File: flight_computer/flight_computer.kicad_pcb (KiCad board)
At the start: 4 copper layers, 47 x 66 mm, 102 parts, among them J1 Conn_02x05_Odd_Even, J2 MEM2061-01-188-00-A_REVA, J3 Conn_01x02, J5 3817564, J7 Conn_01x07_MountingPin, Q1 Q_NPN_BEC, Q2 Q_NMOS_GSD, SW1 SW_Push, SW2 SW_Push, U1 STM8S007C8T6TR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

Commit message: a routing attempt
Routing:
- net /SPI_SCK: track 0.00 -> 50.1 mm, vias 0 -> 3
- net /SCL: track 2.18 -> 50.0 mm, vias 0 -> 2
- net /Microcontroller/SWIM: track 0.00 -> 40.9 mm, vias 0 -> 2
- net /IMU_FSYNC: track 0.00 -> 39.9 mm, vias 0 -> 4
- net /IMU_INT: track 0.00 -> 35.5 mm, vias 0 -> 2
- net /Microcontroller/SPI_MOSI: track 0.00 -> 35.1 mm, vias 0 -> 3
- net /PRESSURE_INT: track 0.00 -> 31.3 mm, vias 0 -> 2
- net GND: track 68.4 -> 97.2 mm, vias 31 -> 55
- net /Microcontroller/SPI_NSS: track 0.00 -> 27.6 mm
- net /SPI_MISO: track 0.00 -> 22.9 mm
- net /Temperature sensor/T+: track 0.00 -> 18.9 mm
- net /Microcontroller/BUTTON: track 0.00 -> 14.1 mm
- net /SDA: track 1.96 -> 9.91 mm
- net /Temperature sensor/T-: track 0.00 -> 7.71 mm
- net /TC_CS: track 0.00 -> 6.70 mm
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
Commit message: Most of the way through relayout and new antenna
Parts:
- removed AE1: Antenna_Chip, my_footprints:ANT_ANT8010LL05R1516A_PUL
- added C39: 100nF, Capacitor_SMD:C_0402_1005Metric, F.Cu at (112.7, 92.5)
- added C40: 0.2pF, Capacitor_SMD:C_0402_1005Metric, F.Cu at (156.6, 101.0)
- added C41: 0.2pF, Capacitor_SMD:C_0402_1005Metric, F.Cu at (159.4, 101.0)
- added L3: 3.9nH, Inductor_SMD:L_0402_1005Metric, F.Cu at (158.0, 100.6)
- added R26: 10k, Resistor_SMD:R_0402_1005Metric, F.Cu at (109.8, 92.5)
- added R27: 10k, Resistor_SMD:R_0402_1005Metric, F.Cu at (109.8, 94.5)
- added R28: 10k, Resistor_SMD:R_0402_1005Metric, F.Cu at (109.8, 96.5)
- added R29: 10k, Resistor_SMD:R_0402_1005Metric, F.Cu at (109.8, 98.5)
- added R30: 10k, Resistor_SMD:R_0402_1005Metric, F.Cu at (109.8, 100.5)
- added U9: Antenna_GPS, my_footprints:1582AT54A0045, F.Cu at (168.7, 93.0)
- moved R21 44.7 mm to (156.9, 133.2), turned to 0 degrees
- moved C38 43.8 mm to (143.4, 133.2), turned to 180 degrees
- moved R23 42.4 mm to (154.4, 133.2), turned to 0 degrees
- moved BZ1 41.3 mm to (127.7, 114.5), turned to 0 degrees
- moved D4 38.3 mm to (148.0, 132.9), turned to 180 degrees
- moved R22 38.2 mm to (145.5, 133.2), turned to 180 degrees
- moved R8 37.1 mm to (123.9, 110.0)
- moved Q1 34.9 mm to (133.1, 119.7), turned to 90 degrees
- moved R7 34.8 mm to (130.9, 120.8), turned to -90 degrees
- moved TP2 30.7 mm to (97.5, 102.1)
- moved C3 25.0 mm to (142.1, 124.3), turned to 0 degrees
- moved TP1 24.5 mm to (153.8, 115.3)
- moved TP3 24.5 mm to (153.8, 118.9)
- moved R4 23.5 mm to (144.5, 124.2), turned to 90 degrees
- moved C22 23.5 mm to (137.6, 125.0)
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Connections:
- J2 pad 1: unconnected-(J2-DAT2-Pad1) -> Net-(J2-DAT2)
- J2 pad 8: unconnected-(J2-DAT1-Pad8) -> Net-(J2-DAT1)
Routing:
- net /Microcontroller/NRST: track 2.21 -> 45.0 mm, vias 1 -> 3
- net /IMU_FSYNC: track 39.9 -> 1.08 mm, vias 4 -> 1
- net /IMU_INT: track 35.5 -> 0.65 mm, vias 2 -> 1
- net /PRESSURE_INT: track 31.3 -> 1.18 mm, vias 2 -> 0
- net /SDA: track 9.91 -> 39.6 mm
- net /Microcontroller/SPI_NSS: track 27.6 -> 0.00 mm
- net /Microcontroller/SWIM: track 40.9 -> 16.0 mm, vias 2 -> 1
- net /GPS_TXD: track 2.32 -> 25.7 mm, vias 0 -> 4
- net /GPS_RXD: track 2.21 -> 24.1 mm, vias 0 -> 2
- net /RADIO_RXD: track 0.00 -> 19.6 mm, vias 0 -> 2
- net /RADIO_M0: track 2.35 -> 20.3 mm
- net /RADIO_TXD: track 0.00 -> 17.7 mm, vias 0 -> 1
- net /SPI_MISO: track 22.9 -> 38.4 mm
- net /RADIO_M1: track 2.34 -> 17.4 mm
- net /SCL: track 50.0 -> 35.7 mm, vias 2 -> 4
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- added copper zone on In2.Cu, net /Power/3V3A
- removed copper zone on B.Cu, net /Power/3V3A

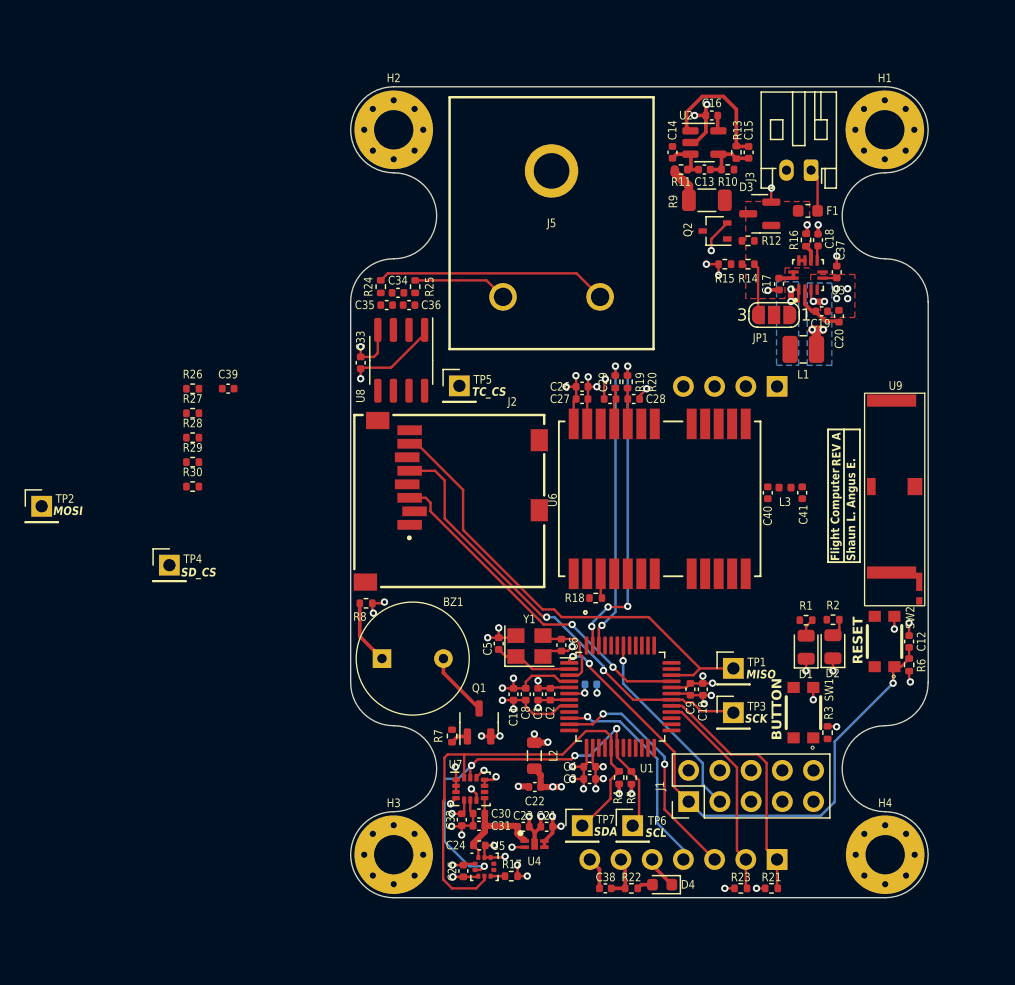
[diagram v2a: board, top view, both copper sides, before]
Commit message: Antenna routing, and other routing done
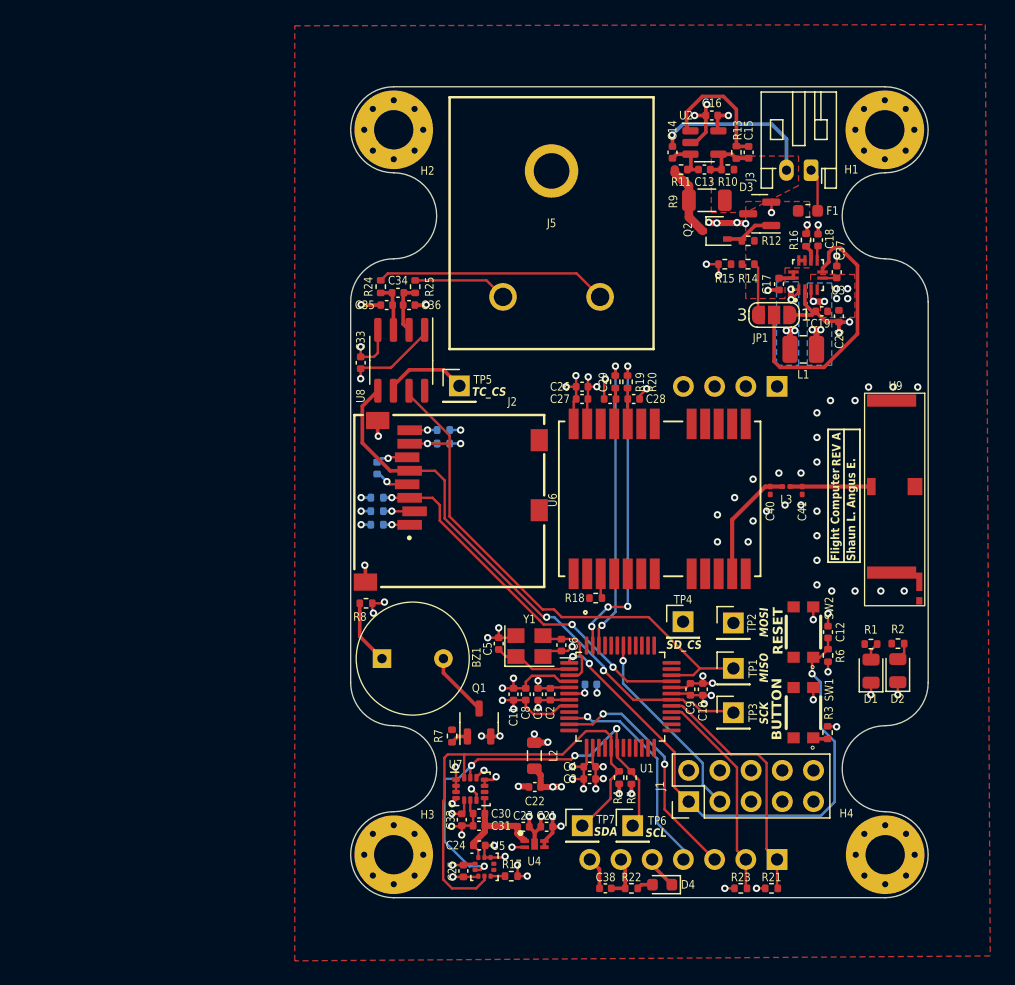
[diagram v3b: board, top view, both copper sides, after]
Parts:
- C39, R26, R27, R28, R29, R30: moved to B.Cu
- C40, C41: footprint Capacitor_SMD:C_0402_1005Metric -> Capacitor_SMD:C_0201_0603Metric
- L3: footprint Inductor_SMD:L_0402_1005Metric -> Inductor_SMD:L_0201_0603Metric
- moved TP2 57.1 mm to (153.8, 111.6)
- moved TP4 42.1 mm to (149.7, 111.5)
- moved R26 20.9 mm to (130.2, 97.0)
- moved R27 20.5 mm to (130.2, 95.9)
- moved R28 16.6 mm to (124.8, 103.6), turned to 180 degrees
- moved R29 15.5 mm to (124.8, 102.5), turned to 180 degrees
- moved R30 15.0 mm to (124.8, 101.4), turned to 180 degrees
- moved C39 13.7 mm to (124.8, 99.0), turned to 90 degrees
- moved C12 6.64 mm to (161.5, 112.3)
- moved R6 6.64 mm to (161.5, 114.2)
- moved SW2 6.64 mm to (159.5, 112.3)
- moved D2 5.63 mm to (167.2, 115.5)
- moved D1 5.63 mm to (165.0, 115.5)
- moved R1 5.63 mm to (165.0, 113.3)
- moved R2 5.63 mm to (167.2, 113.3)
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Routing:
- net /Power/3V3A: track 13.4 -> 109.1 mm, vias 7 -> 8
- net Net-(JP1-C): track 0.00 -> 22.3 mm
- net /Power/BAT_GND: track 0.00 -> 13.7 mm, vias 0 -> 1
- net GND: track 92.0 -> 103.8 mm, vias 48 -> 85
- net Net-(U6-RF_IN): track 0.00 -> 9.60 mm
- net /SPI_SCK: track 36.5 -> 46.1 mm
- net /SPI_MISO: track 38.4 -> 46.4 mm, vias 0 -> 1
- net /TC_CS: track 0.00 -> 6.85 mm
- net /Microcontroller/3V3D: track 40.8 -> 47.6 mm, vias 24 -> 30
- net Net-(U9-Feed): track 0.00 -> 6.61 mm
- net Net-(D3-K): track 0.00 -> 4.26 mm
- net Net-(U8-T-): track 0.00 -> 4.17 mm
- net Net-(U8-T+): track 0.00 -> 3.99 mm
- net /Power/I_{sense_raw}: track 3.02 -> 5.99 mm
- net /Microcontroller/SPI_NSS: track 0.00 -> 2.55 mm, vias 0 -> 1
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- added copper zone on F.Cu, net /Power/BAT_GND
- added copper zone on F.Cu, net GND
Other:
- board text added: "0.1521 controlled impedance trace width For JLC04161H-3313 4 layer stackup Ref plane L2, siglan L1 1oz outer, 0.5oz inner coplanar waveguide with 0.25mm to waveguide"
- board text added: "0.3421 mm controlled impedance trace width For JLC04161H-7628 4 layer stackup 1.6mm Signal L1, ref plane L2 1oz outer, 0.0152mm inner coplanar waveguide with 0.5mm to waveguide pour"
- board text added: "0.6431 mm controlled impedance trace width For JLC04161H-7628B 4 layer stackup Signal L1, ref plane L2 1oz outer, 0.0152mm inner coplanar waveguide with 0.22mm to waveguide"
- board text removed: "0.1565 controlled impedance trace width For JLC04161H-3313 4 layer stackup microstrip"

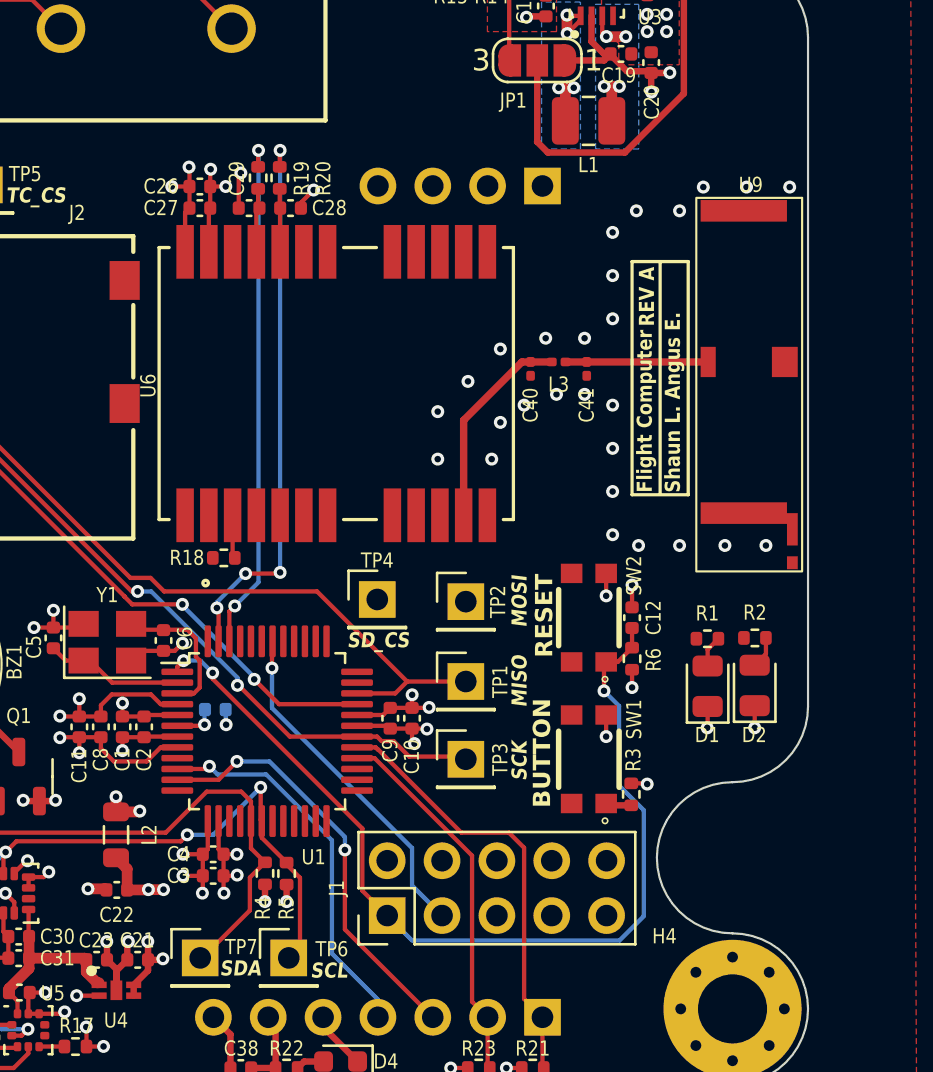
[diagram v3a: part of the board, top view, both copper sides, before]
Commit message: Moving antenna and removing matching circuit
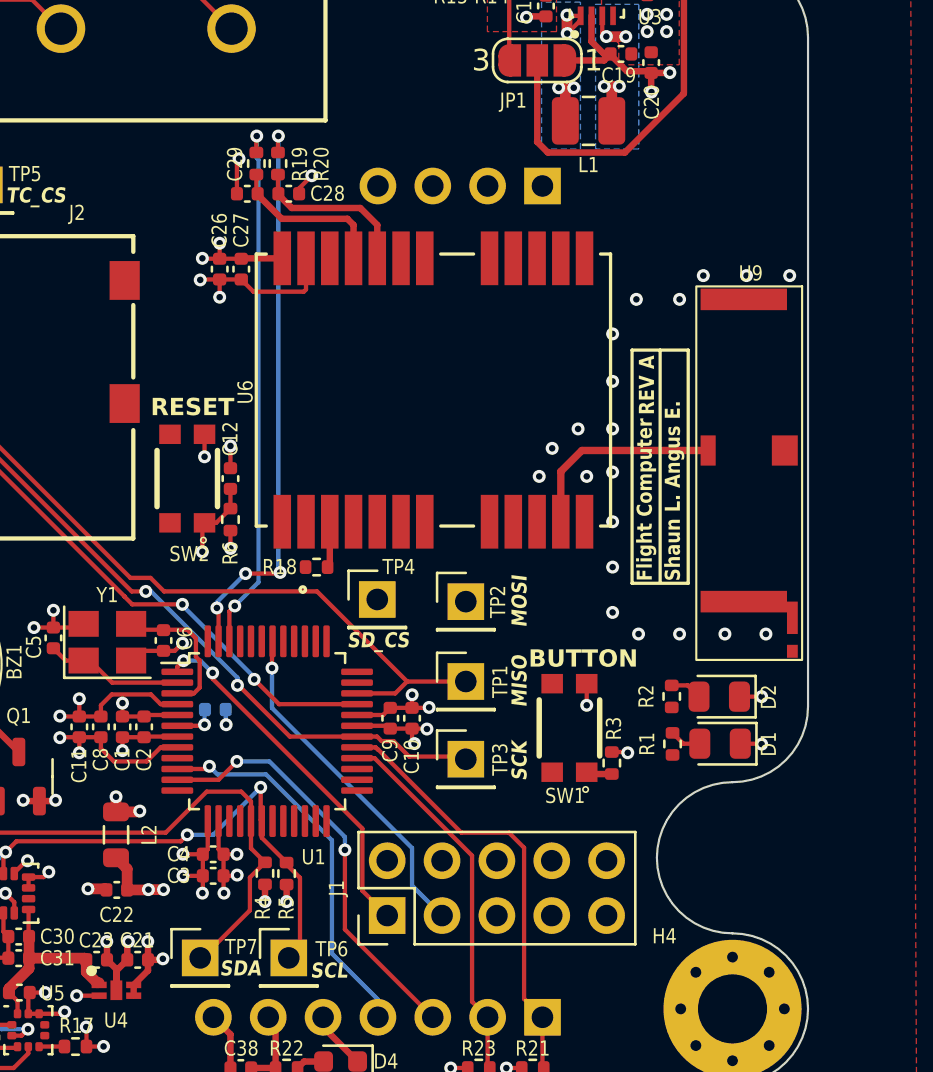
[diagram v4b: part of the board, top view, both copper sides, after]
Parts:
- removed C40, C41: 0.2pF, Capacitor_SMD:C_0201_0603Metric
- removed L3: 3.9nH, Inductor_SMD:L_0201_0603Metric
- moved R6 19.7 mm to (142.9, 107.8)
- moved C12 19.7 mm to (142.9, 105.9)
- moved SW2 19.7 mm to (140.9, 105.9)
- moved R1 5.13 mm to (163.4, 118.2), turned to 90 degrees
- moved R2 4.71 mm to (163.3, 116.0), turned to 90 degrees
- moved U6 4.51 mm to (152.3, 101.8)
- moved R18 4.32 mm to (146.9, 110.0)
- moved U9 4.10 mm to (168.7, 97.1)
- moved C26 3.93 mm to (142.4, 96.2), turned to 90 degrees
- moved C27 3.42 mm to (143.4, 96.2), turned to 90 degrees
- moved D1 2.72 mm to (165.6, 118.2), turned to 180 degrees
- moved D2 1.72 mm to (165.5, 116.0), turned to 180 degrees
- moved R3 1.71 mm to (160.6, 119.1)
- moved SW1 1.71 mm to (158.6, 117.5)
- moved C28 0.67 mm to (145.6, 92.7)
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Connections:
- U9 pad 1: Net-(U9-Feed) -> Net-(U6-RF_IN)
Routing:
- net /Microcontroller/NRST: track 44.6 -> 20.6 mm
- net Net-(U9-Feed): track 6.61 -> 0.00 mm
- net Net-(U6-TXD): track 2.93 -> 7.65 mm
- net Net-(U6-RXD): track 3.00 -> 7.72 mm
- net /Microcontroller/3V3D: track 47.6 -> 50.5 mm
- net /Power/3V3A: track 109.1 -> 111.2 mm
- net /GPS_TXD: track 25.7 -> 26.4 mm
- net /GPS_RXD: track 24.1 -> 24.8 mm
- net GND: track 103.8 -> 103.5 mm, vias 85 -> 78

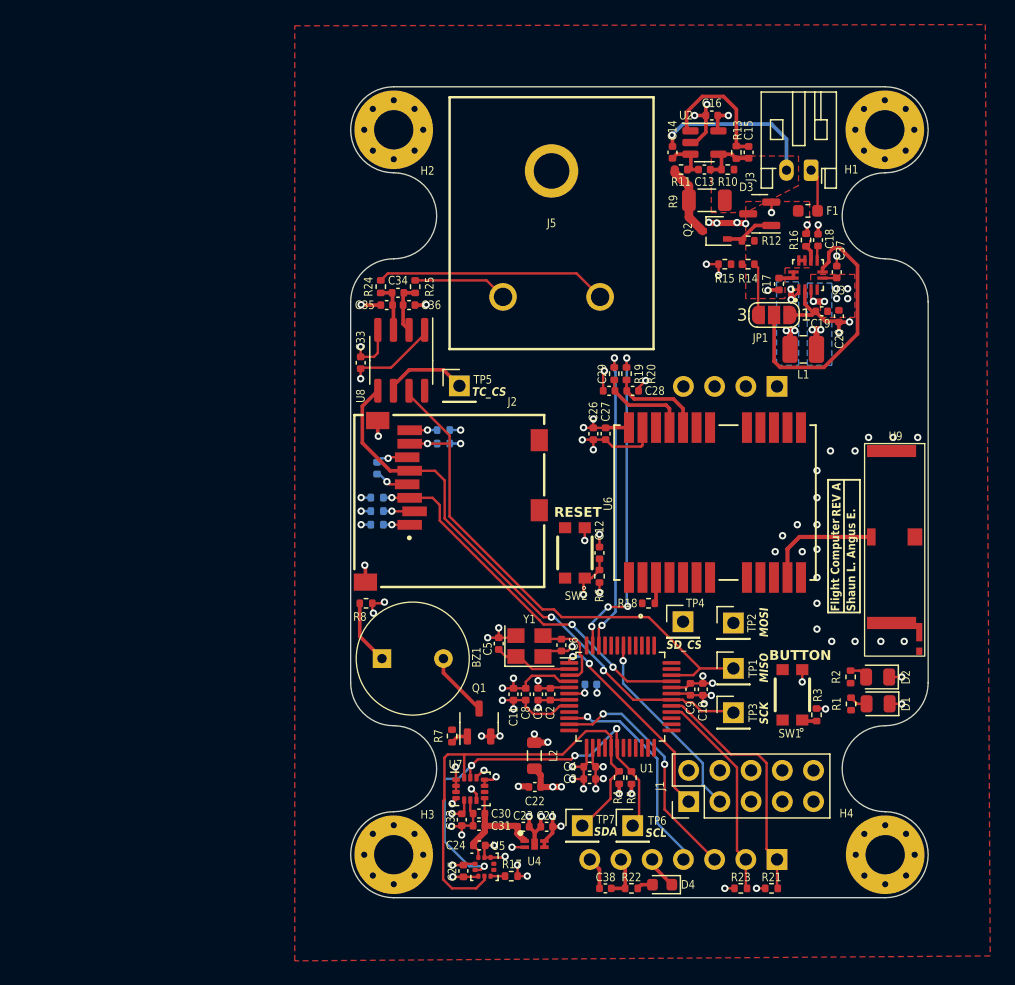
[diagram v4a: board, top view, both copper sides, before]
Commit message: First draft of PCB routing complete
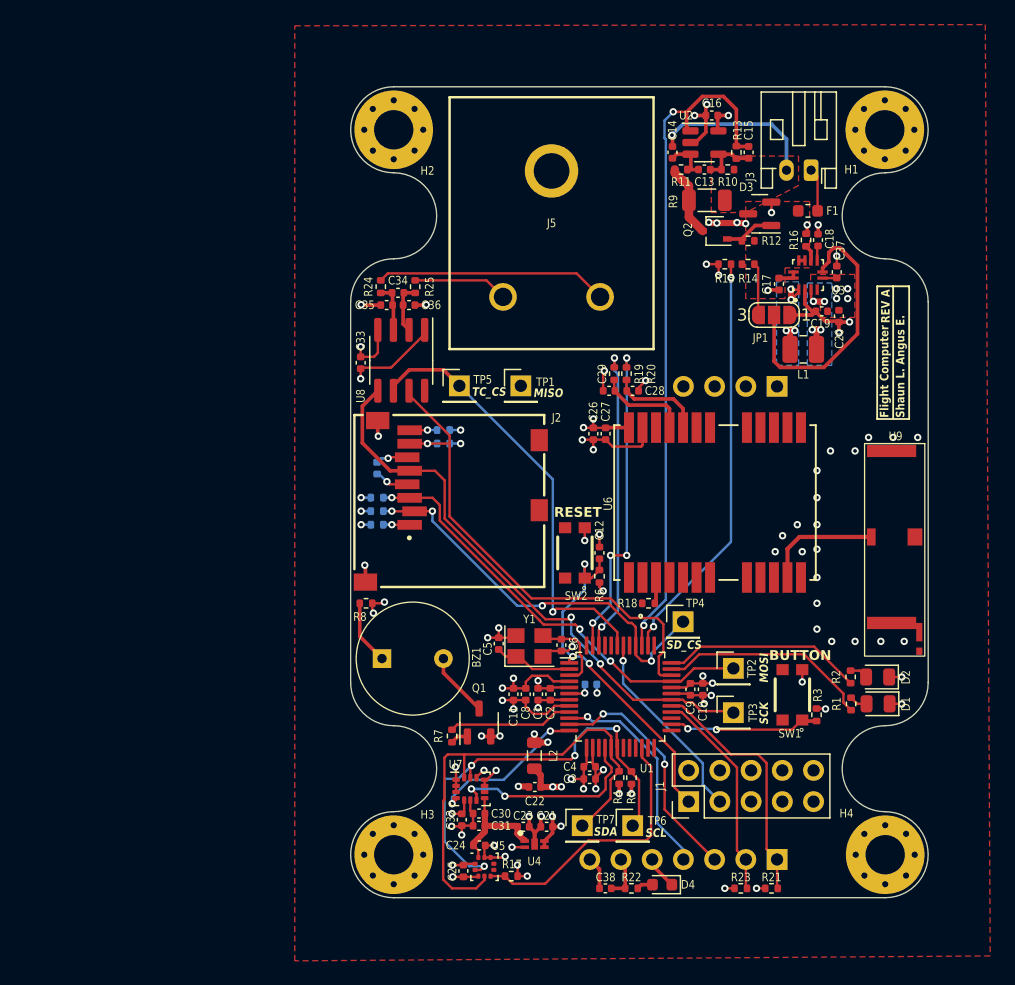
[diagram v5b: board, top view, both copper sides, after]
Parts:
- moved TP1 28.8 mm to (136.5, 92.3)
- moved TP2 3.70 mm to (153.8, 115.3)
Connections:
- U1 pad 12: unconnected-(U1A-PA6-Pad12) -> /IMU_INT
- U1 pad 15: /Microcontroller/I_{SENSE} -> unconnected-(U1A-PB7-Pad15)
- U1 pad 16: /Microcontroller/VBATT_{SENSE} -> /IMU_FSYNC
- U1 pad 22: unconnected-(U1A-PB0-Pad22) -> /PRESSURE_INT
- U1 pad 25: /Microcontroller/SPI_NSS -> unconnected-(U1A-PE5-Pad25)
- U1 pad 26: unconnected-(U1A-PC1-Pad26) -> /Microcontroller/BUTTON
- U1 pad 27: /TC_CS -> unconnected-(U1A-PC2-Pad27)
- U1 pad 35: unconnected-(U1A-PG0-Pad35) -> /Microcontroller/LED_GREEN
- U1 pad 36: unconnected-(U1A-PG1-Pad36) -> /Microcontroller/LED_RED
- U1 pad 37: /Microcontroller/BUZZER_INDICATOR -> unconnected-(U1A-PE3-Pad37)
- U1 pad 38: /Microcontroller/LED_GREEN -> /Microcontroller/VBATT_{SENSE}
- U1 pad 39: /Microcontroller/LED_RED -> /Microcontroller/I_{SENSE}
- U1 pad 40: /Microcontroller/BUTTON -> /Microcontroller/SPI_NSS
- U1 pad 43: /PRESSURE_INT -> /TC_CS
- U1 pad 44: /IMU_FSYNC -> unconnected-(U1A-PD3-Pad44)
- U1 pad 45: /IMU_INT -> unconnected-(U1A-PD4-Pad45)
- U1 pad 9: unconnected-(U1A-PA3-Pad9) -> /Microcontroller/BUZZER_INDICATOR
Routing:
- net /Microcontroller/I_{SENSE}: track 10.7 -> 56.3 mm, vias 0 -> 2
- net /Microcontroller/VBATT_{SENSE}: track 0.00 -> 33.8 mm, vias 0 -> 2
- net /Microcontroller/SPI_NSS: track 2.55 -> 33.1 mm, vias 1 -> 4
- net /TC_CS: track 6.85 -> 35.6 mm, vias 0 -> 1
- net /PRESSURE_INT: track 1.18 -> 22.4 mm
- net /Microcontroller/LED_GREEN: track 0.00 -> 17.4 mm
- net /Microcontroller/LED_RED: track 0.00 -> 16.3 mm
- net /IMU_FSYNC: track 1.08 -> 16.3 mm, vias 1 -> 2
- net /IMU_INT: track 0.59 -> 13.1 mm, vias 1 -> 2
- net /Microcontroller/BUTTON: track 1.20 -> 12.3 mm, vias 0 -> 2
- net /Microcontroller/BUZZER_INDICATOR: track 0.00 -> 10.1 mm
- net /Microcontroller/NRST: track 20.6 -> 29.0 mm
- net /Microcontroller/SPI_MOSI: track 30.5 -> 36.0 mm
- net /SPI_MISO: track 46.4 -> 42.0 mm
- net /SPI_SCK: track 46.1 -> 47.0 mm
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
